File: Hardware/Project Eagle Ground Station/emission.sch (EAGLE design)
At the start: 23 parts

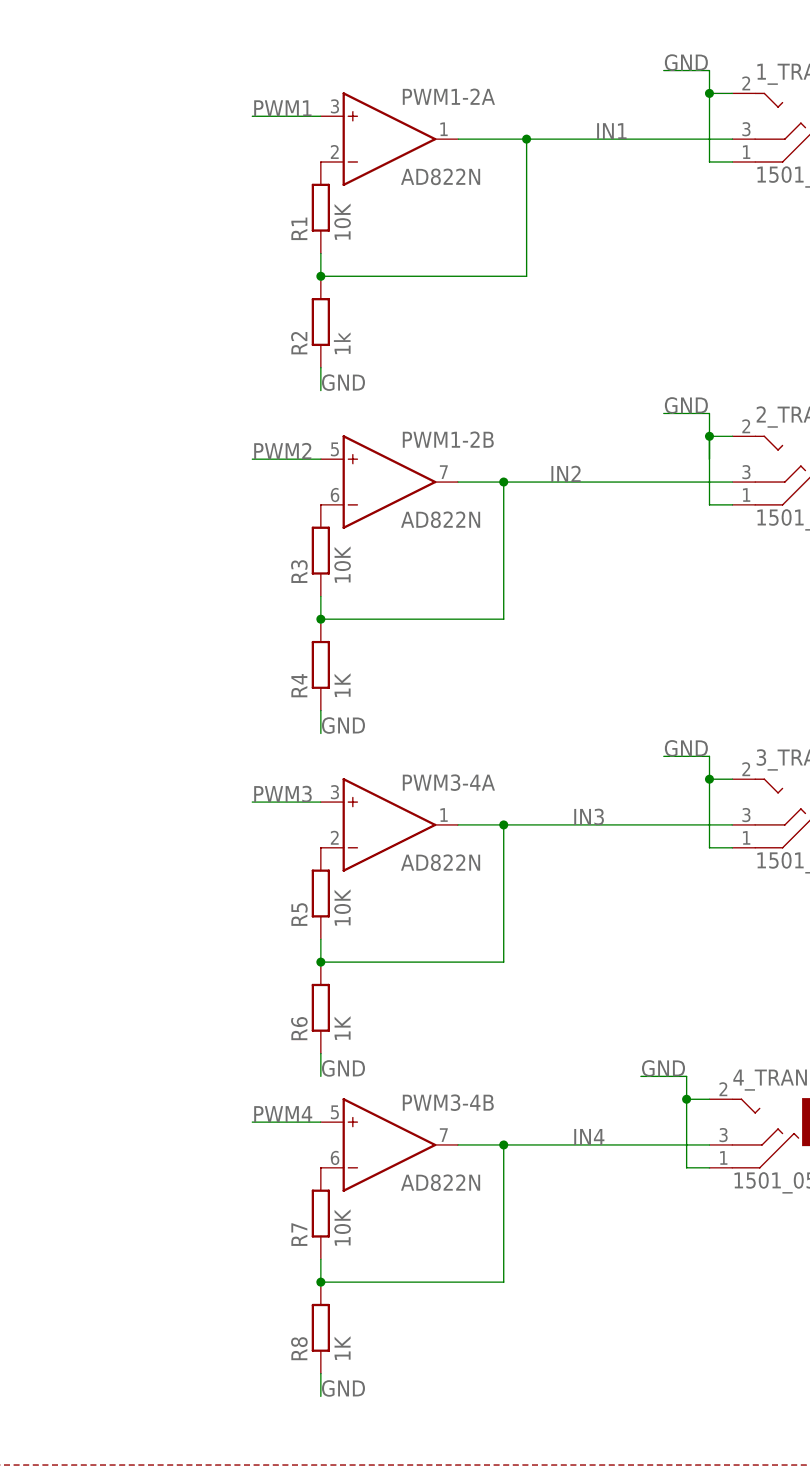
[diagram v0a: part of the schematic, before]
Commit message: Correct the AOP connection
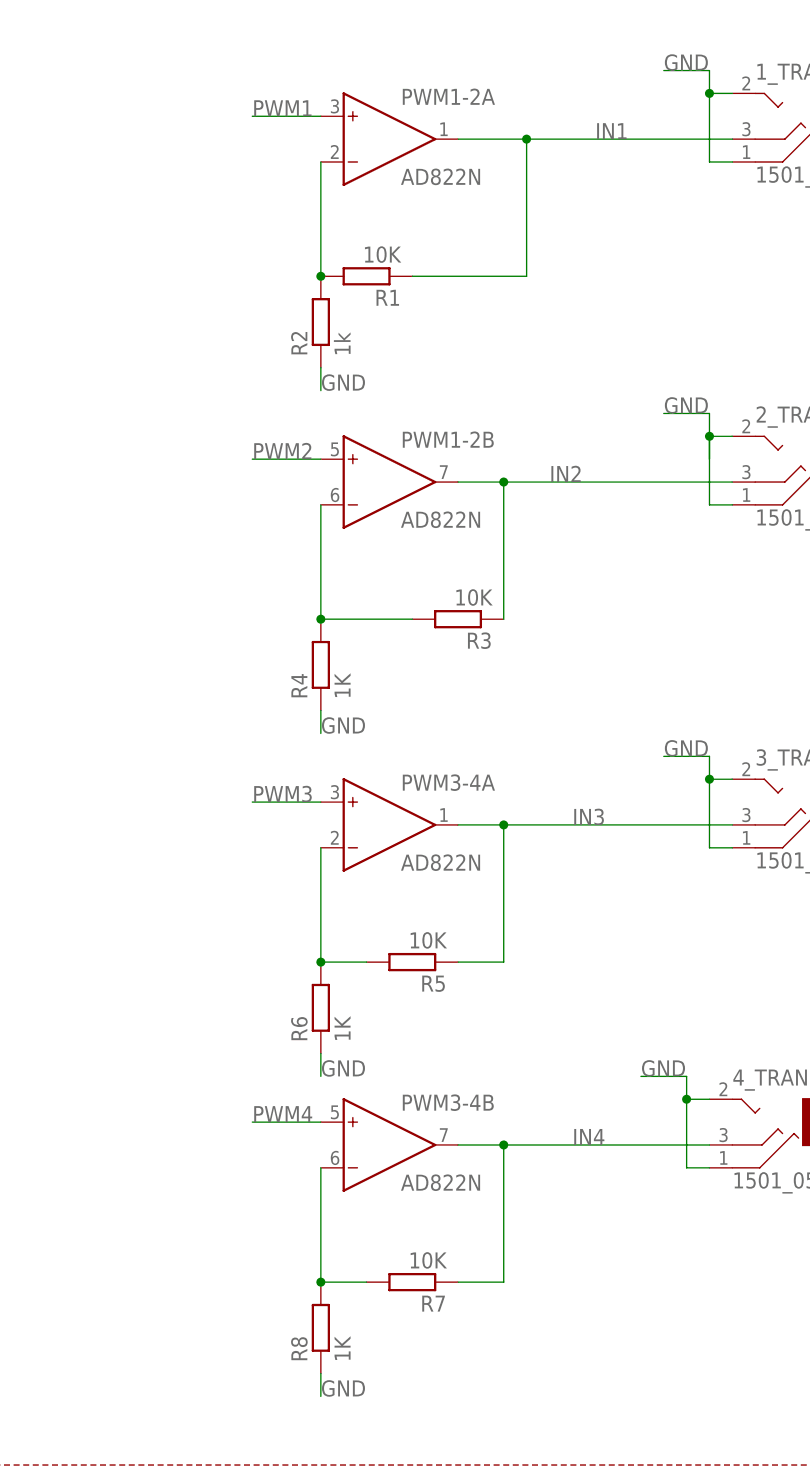
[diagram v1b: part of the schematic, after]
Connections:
- net IN1: no longer R2.2
- net IN2: no longer R4.2
- net IN3: no longer R6.2
- net IN4: no longer R8.2
- net N$1: now also R2.2
- net N$2: now also R4.2
- net N$4: now also R6.2
- net N$5: now also R8.2
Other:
- moved on the sheet: R1, R3, R5, R7
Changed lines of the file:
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@@
 <instance part="3_TRANSDUCER" gate="G$1" x="93.98" y="7.62"/>
 <instance part="4_TRANSDUCER" gate="G$1" x="91.44" y="-27.94"/>
-<instance part="R1" gate="G$1" x="43.18" y="73.66" rot="R90"/>
+<instance part="R1" gate="G$1" x="48.26" y="66.04" rot="R180"/>
 <instance part="R2" gate="G$1" x="43.18" y="60.96" rot="R90"/>
-<instance part="R3" gate="G$1" x="43.18" y="35.56" rot="R90"/>
+<instance part="R3" gate="G$1" x="58.42" y="27.94" rot="R180"/>
 <instance part="R4" gate="G$1" x="43.18" y="22.86" rot="R90"/>
 <instance part="C1" gate="G$1" x="-96.52" y="38.1"/>
 <instance part="C2" gate="G$1" x="-58.42" y="38.1"/>
 <instance part="SUPPLY" gate="G$1" x="-157.48" y="88.9"/>
-<instance part="R5" gate="G$1" x="43.18" y="-2.54" rot="R90"/>
+<instance part="R5" gate="G$1" x="53.34" y="-10.16" rot="R180"/>
 <instance part="R6" gate="G$1" x="43.18" y="-15.24" rot="R90"/>
-<instance part="R7" gate="G$1" x="43.18" y="-38.1" rot="R90"/>
+<instance part="R7" gate="G$1" x="53.34" y="-45.72" rot="R180"/>
 <instance part="R8" gate="G$1" x="43.18" y="-50.8" rot="R90"/>
 <instance part="U$2" gate="G$1" x="-104.14" y="93.98" rot="R270"/>
@@
 <wire x1="58.42" y1="81.28" x2="66.04" y2="81.28" width="0.1524" layer="91"/>
 <wire x1="66.04" y1="81.28" x2="66.04" y2="66.04" width="0.1524" layer="91"/>
-<wire x1="66.04" y1="66.04" x2="43.18" y2="66.04" width="0.1524" layer="91"/>
 <junction x="66.04" y="81.28"/>
 <label x="73.66" y="81.28" size="1.778" layer="95"/>
 <wire x1="66.04" y1="81.28" x2="88.9" y2="81.28" width="0.1524" layer="91"/>
-<wire x1="43.18" y1="66.04" x2="43.18" y2="68.58" width="0.1524" layer="91"/>
 <pinref part="1_TRANSDUCER" gate="G$1" pin="3"/>
 <pinref part="R1" gate="G$1" pin="1"/>
-<pinref part="R2" gate="G$1" pin="2"/>
-<junction x="43.18" y="66.04"/>
+<wire x1="53.34" y1="66.04" x2="66.04" y2="66.04" width="0.1524" layer="91"/>
 </segment>
 </net>
@@
 <net name="IN2" class="0">
 <segment>
-<wire x1="43.18" y1="27.94" x2="63.5" y2="27.94" width="0.1524" layer="91"/>
 <wire x1="63.5" y1="27.94" x2="63.5" y2="43.18" width="0.1524" layer="91"/>
 <pinref part="PWM1-2" gate="B" pin="OUT"/>
@@
 <label x="68.58" y="43.18" size="1.778" layer="95"/>
 <wire x1="63.5" y1="43.18" x2="88.9" y2="43.18" width="0.1524" layer="91"/>
-<wire x1="43.18" y1="27.94" x2="43.18" y2="30.48" width="0.1524" layer="91"/>
 <pinref part="2_TRANSDUCER" gate="G$1" pin="3"/>
 <pinref part="R3" gate="G$1" pin="1"/>
-<pinref part="R4" gate="G$1" pin="2"/>
-<junction x="43.18" y="27.94"/>
 </segment>
 </net>
@@
 <pinref part="PWM3-4" gate="A" pin="OUT"/>
 <wire x1="58.42" y1="5.08" x2="63.5" y2="5.08" width="0.1524" layer="91"/>
-<wire x1="43.18" y1="-10.16" x2="63.5" y2="-10.16" width="0.1524" layer="91"/>
 <wire x1="63.5" y1="-10.16" x2="63.5" y2="5.08" width="0.1524" layer="91"/>
 <junction x="63.5" y="5.08"/>
 <label x="71.12" y="5.08" size="1.778" layer="95"/>
 <wire x1="63.5" y1="5.08" x2="88.9" y2="5.08" width="0.1524" layer="91"/>
-<wire x1="43.18" y1="-10.16" x2="43.18" y2="-7.62" width="0.1524" layer="91"/>
 <pinref part="3_TRANSDUCER" gate="G$1" pin="3"/>
-<pinref part="R6" gate="G$1" pin="2"/>
-<junction x="43.18" y="-10.16"/>
 <pinref part="R5" gate="G$1" pin="1"/>
+<wire x1="63.5" y1="-10.16" x2="58.42" y2="-10.16" width="0.1524" layer="91"/>
 </segment>
 </net>
@@
 <pinref part="PWM3-4" gate="B" pin="OUT"/>
 <wire x1="58.42" y1="-30.48" x2="63.5" y2="-30.48" width="0.1524" layer="91"/>
-<wire x1="43.18" y1="-45.72" x2="63.5" y2="-45.72" width="0.1524" layer="91"/>
 <wire x1="63.5" y1="-45.72" x2="63.5" y2="-30.48" width="0.1524" layer="91"/>
 <junction x="63.5" y="-30.48"/>
 <label x="71.12" y="-30.48" size="1.778" layer="95"/>
 <wire x1="63.5" y1="-30.48" x2="86.36" y2="-30.48" width="0.1524" layer="91"/>
-<wire x1="43.18" y1="-45.72" x2="43.18" y2="-43.18" width="0.1524" layer="91"/>
 <pinref part="4_TRANSDUCER" gate="G$1" pin="3"/>
 <pinref part="R7" gate="G$1" pin="1"/>
-<pinref part="R8" gate="G$1" pin="2"/>
-<junction x="43.18" y="-45.72"/>
+<wire x1="58.42" y1="-45.72" x2="63.5" y2="-45.72" width="0.1524" layer="91"/>
 </segment>
 </net>
@@
 <pinref part="PWM1-2" gate="A" pin="IN-"/>
 <pinref part="R1" gate="G$1" pin="2"/>
+<wire x1="43.18" y1="66.04" x2="43.18" y2="78.74" width="0.1524" layer="91"/>
+<pinref part="R2" gate="G$1" pin="2"/>
+<junction x="43.18" y="66.04"/>
 </segment>
 </net>
 <net name="N$2" class="0">
 <segment>
+<pinref part="R3" gate="G$1" pin="2"/>
+<pinref part="R4" gate="G$1" pin="2"/>
+<wire x1="53.34" y1="27.94" x2="43.18" y2="27.94" width="0.1524" layer="91"/>
 <pinref part="PWM1-2" gate="B" pin="IN-"/>
-<pinref part="R3" gate="G$1" pin="2"/>
+<wire x1="43.18" y1="27.94" x2="43.18" y2="40.64" width="0.1524" layer="91"/>
+<junction x="43.18" y="27.94"/>
 </segment>
 </net>
 <net name="N$4" class="0">
 <segment>
+<pinref part="R5" gate="G$1" pin="2"/>
+<pinref part="R6" gate="G$1" pin="2"/>
+<wire x1="48.26" y1="-10.16" x2="43.18" y2="-10.16" width="0.1524" layer="91"/>
 <pinref part="PWM3-4" gate="A" pin="IN-"/>
-<pinref part="R5" gate="G$1" pin="2"/>
+<wire x1="43.18" y1="-10.16" x2="43.18" y2="2.54" width="0.1524" layer="91"/>
+<junction x="43.18" y="-10.16"/>
 </segment>
 </net>
@@
 <segment>
 <pinref part="PWM3-4" gate="B" pin="IN-"/>
+<wire x1="43.18" y1="-33.02" x2="43.18" y2="-45.72" width="0.1524" layer="91"/>
 <pinref part="R7" gate="G$1" pin="2"/>
-</segment>
-</net>
+<wire x1="43.18" y1="-45.72" x2="48.26" y2="-45.72" width="0.1524" layer="91"/>
+<pinref part="R8" gate="G$1" pin="2"/>
+<junction x="43.18" y="-45.72"/>
+</segment>
+</net>
